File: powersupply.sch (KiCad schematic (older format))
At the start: 18 parts, among them P1 PWR, P2 PWR_SW, U1 LM7805, U2 LM3940

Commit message: Everything associated except joystick
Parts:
- F1: footprint (none) -> SMD_Packages:SMD-1812_l
- P2: footprint (none) -> nu9j-footprints:PWR2-16AWG
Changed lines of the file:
@@
 F 0 "P2" V 3700 2200 40  0000 C CNN
 F 1 "PWR_SW" V 3800 2200 40  0000 C CNN
-F 2 "" H 3750 2200 60  0001 C CNN
+F 2 "nu9j-footprints:PWR2-16AWG" H 3750 2200 60  0001 C CNN
 F 3 "" H 3750 2200 60  0000 C CNN
 	1    3750 2200
@@
 	3300 2550 3650 2550
 $Comp
-L GND #PWR20
+L GND #PWR020
 U 1 1 5470C747
 P 3100 2700
-F 0 "#PWR20" H 3100 2700 30  0001 C CNN
+F 0 "#PWR020" H 3100 2700 30  0001 C CNN
 F 1 "GND" H 3100 2630 30  0001 C CNN
 F 2 "" H 3100 2700 60  0000 C CNN
@@
 $EndComp
 $Comp
-L GND #PWR25
+L GND #PWR021
 U 1 1 5470C830
 P 4450 3000
-F 0 "#PWR25" H 4450 3000 30  0001 C CNN
+F 0 "#PWR021" H 4450 3000 30  0001 C CNN
 F 1 "GND" H 4450 2930 30  0001 C CNN
 F 2 "" H 4450 3000 60  0000 C CNN
@@
 $EndComp
 $Comp
-L GND #PWR26
+L GND #PWR022
 U 1 1 5470C83B
 P 4750 3000
-F 0 "#PWR26" H 4750 3000 30  0001 C CNN
+F 0 "#PWR022" H 4750 3000 30  0001 C CNN
 F 1 "GND" H 4750 2930 30  0001 C CNN
 F 2 "" H 4750 3000 60  0000 C CNN
@@
 	4750 2950 4750 3000
 $Comp
-L +12V #PWR39
+L +12V #PWR023
 U 1 1 5470C933
 P 7600 2500
-F 0 "#PWR39" H 7600 2450 20  0001 C CNN
+F 0 "#PWR023" H 7600 2450 20  0001 C CNN
 F 1 "+12V" H 7600 2600 30  0000 C CNN
 F 2 "" H 7600 2500 60  0000 C CNN
@@
 F 0 "F1" H 7250 2600 40  0000 C CNN
 F 1 "PTS181224V150" H 7050 2500 40  0000 C CNN
-F 2 "" H 7150 2550 60  0001 C CNN
+F 2 "SMD_Packages:SMD-1812_l" H 7150 2550 60  0001 C CNN
 F 3 "" H 7150 2550 60  0000 C CNN
 	1    7150 2550
@@
 	7600 2550 7600 2500
 $Comp
-L GND #PWR22
+L GND #PWR024
 U 1 1 5470CBF4
 P 3900 4250
-F 0 "#PWR22" H 3900 4250 30  0001 C CNN
+F 0 "#PWR024" H 3900 4250 30  0001 C CNN
 F 1 "GND" H 3900 4180 30  0001 C CNN
 F 2 "" H 3900 4250 60  0000 C CNN
@@
 $EndComp
 $Comp
-L GND #PWR31
+L GND #PWR025
 U 1 1 5470CBFF
 P 5750 4250
-F 0 "#PWR31" H 5750 4250 30  0001 C CNN
+F 0 "#PWR025" H 5750 4250 30  0001 C CNN
 F 1 "GND" H 5750 4180 30  0001 C CNN
 F 2 "" H 5750 4250 60  0000 C CNN
@@
 $EndComp
 $Comp
-L +12V #PWR21
+L +12V #PWR026
 U 1 1 5470CC17
 P 3500 3950
-F 0 "#PWR21" H 3500 3900 20  0001 C CNN
+F 0 "#PWR026" H 3500 3900 20  0001 C CNN
 F 1 "+12V" H 3500 4050 30  0000 C CNN
 F 2 "" H 3500 3950 60  0000 C CNN
@@
 $EndComp
 $Comp
-L +5V #PWR23
+L +5V #PWR027
 U 1 1 5470CC25
 P 4300 3950
-F 0 "#PWR23" H 4300 4040 20  0001 C CNN
+F 0 "#PWR027" H 4300 4040 20  0001 C CNN
 F 1 "+5V" H 4300 4040 30  0000 C CNN
 F 2 "" H 4300 3950 60  0000 C CNN
@@
 $EndComp
 $Comp
-L +5V #PWR29
+L +5V #PWR028
 U 1 1 5470CC37
 P 5350 3950
-F 0 "#PWR29" H 5350 4040 20  0001 C CNN
+F 0 "#PWR028" H 5350 4040 20  0001 C CNN
 F 1 "+5V" H 5350 4040 30  0000 C CNN
 F 2 "" H 5350 3950 60  0000 C CNN
@@
 $EndComp
 $Comp
-L +3.3V #PWR34
+L +3.3V #PWR029
 U 1 1 5470CC44
 P 6150 3950
-F 0 "#PWR34" H 6150 3910 30  0001 C CNN
+F 0 "#PWR029" H 6150 3910 30  0001 C CNN
 F 1 "+3.3V" H 6150 4060 30  0000 C CNN
 F 2 "" H 6150 3950 60  0000 C CNN
@@
 $EndComp
 $Comp
-L GND #PWR24
+L GND #PWR030
 U 1 1 5470CCF4
 P 4300 4350
-F 0 "#PWR24" H 4300 4350 30  0001 C CNN
+F 0 "#PWR030" H 4300 4350 30  0001 C CNN
 F 1 "GND" H 4300 4280 30  0001 C CNN
 F 2 "" H 4300 4350 60  0000 C CNN
@@
 $EndComp
 $Comp
-L GND #PWR35
+L GND #PWR031
 U 1 1 5470CCFF
 P 6150 4350
-F 0 "#PWR35" H 6150 4350 30  0001 C CNN
+F 0 "#PWR031" H 6150 4350 30  0001 C CNN
 F 1 "GND" H 6150 4280 30  0001 C CNN
 F 2 "" H 6150 4350 60  0000 C CNN
@@
 $EndComp
 $Comp
-L GND #PWR27
+L GND #PWR032
 U 1 1 54789812
 P 5050 3000
-F 0 "#PWR27" H 5050 3000 30  0001 C CNN
+F 0 "#PWR032" H 5050 3000 30  0001 C CNN
 F 1 "GND" H 5050 2930 30  0001 C CNN
 F 2 "" H 5050 3000 60  0000 C CNN
@@
 $EndComp
 $Comp
-L GND #PWR28
+L GND #PWR033
 U 1 1 5478981D
 P 5350 3000
-F 0 "#PWR28" H 5350 3000 30  0001 C CNN
+F 0 "#PWR033" H 5350 3000 30  0001 C CNN
 F 1 "GND" H 5350 2930 30  0001 C CNN
 F 2 "" H 5350 3000 60  0000 C CNN
@@
 $EndComp
 $Comp
-L GND #PWR30
+L GND #PWR034
 U 1 1 54789828
 P 5650 3000
-F 0 "#PWR30" H 5650 3000 30  0001 C CNN
+F 0 "#PWR034" H 5650 3000 30  0001 C CNN
 F 1 "GND" H 5650 2930 30  0001 C CNN
 F 2 "" H 5650 3000 60  0000 C CNN
@@
 $EndComp
 $Comp
-L GND #PWR32
+L GND #PWR035
 U 1 1 54789833
 P 5900 3000
-F 0 "#PWR32" H 5900 3000 30  0001 C CNN
+F 0 "#PWR035" H 5900 3000 30  0001 C CNN
 F 1 "GND" H 5900 2930 30  0001 C CNN
 F 2 "" H 5900 3000 60  0000 C CNN
@@
 $EndComp
 $Comp
-L GND #PWR33
+L GND #PWR036
 U 1 1 5478983E
 P 6100 3000
-F 0 "#PWR33" H 6100 3000 30  0001 C CNN
+F 0 "#PWR036" H 6100 3000 30  0001 C CNN
 F 1 "GND" H 6100 2930 30  0001 C CNN
 F 2 "" H 6100 3000 60  0000 C CNN
@@
 $EndComp
 $Comp
-L GND #PWR36
+L GND #PWR037
 U 1 1 54789849
 P 6300 3000
-F 0 "#PWR36" H 6300 3000 30  0001 C CNN
+F 0 "#PWR037" H 6300 3000 30  0001 C CNN
 F 1 "GND" H 6300 2930 30  0001 C CNN
 F 2 "" H 6300 3000 60  0000 C CNN
@@
 $EndComp
 $Comp
-L GND #PWR37
+L GND #PWR038
 U 1 1 54789854
 P 6500 3000
-F 0 "#PWR37" H 6500 3000 30  0001 C CNN
+F 0 "#PWR038" H 6500 3000 30  0001 C CNN
 F 1 "GND" H 6500 2930 30  0001 C CNN
 F 2 "" H 6500 3000 60  0000 C CNN
@@
 $EndComp
 $Comp
-L GND #PWR38
+L GND #PWR039
 U 1 1 5478985F
 P 6700 3000
-F 0 "#PWR38" H 6700 3000 30  0001 C CNN
+F 0 "#PWR039" H 6700 3000 30  0001 C CNN
 F 1 "GND" H 6700 2930 30  0001 C CNN
 F 2 "" H 6700 3000 60  0000 C CNN

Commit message: Fixed pin assignment issues in pcb layout
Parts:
- U1: footprint SMD_Packages:DPAK-2 -> nu9j-footprints:DPAK-3_VIVOGND
- U2: footprint SMD_Packages:TO-263 -> nu9j-footprints:TO-263_VIVOGND
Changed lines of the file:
@@
 F 0 "U1" H 4050 3804 60  0000 C CNN
 F 1 "LM7805" H 3900 4200 60  0000 C CNN
-F 2 "SMD_Packages:DPAK-2" H 3900 4000 60  0001 C CNN
+F 2 "nu9j-footprints:DPAK-3_VIVOGND" H 3900 4000 60  0001 C CNN
 F 3 "" H 3900 4000 60  0000 C CNN
 	1    3900 4000
@@
 F 0 "U2" H 5900 3804 60  0000 C CNN
 F 1 "LM3940" H 5750 4200 60  0000 C CNN
-F 2 "SMD_Packages:TO-263" H 5750 4000 60  0001 C CNN
+F 2 "nu9j-footprints:TO-263_VIVOGND" H 5750 4000 60  0001 C CNN
 F 3 "" H 5750 4000 60  0000 C CNN
 	1    5750 4000

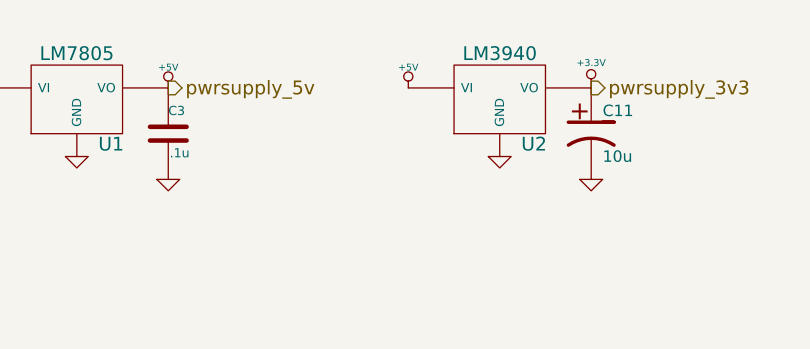
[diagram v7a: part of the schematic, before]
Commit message: Separate analog/digital gnd. Add some filtering caps and reset button.
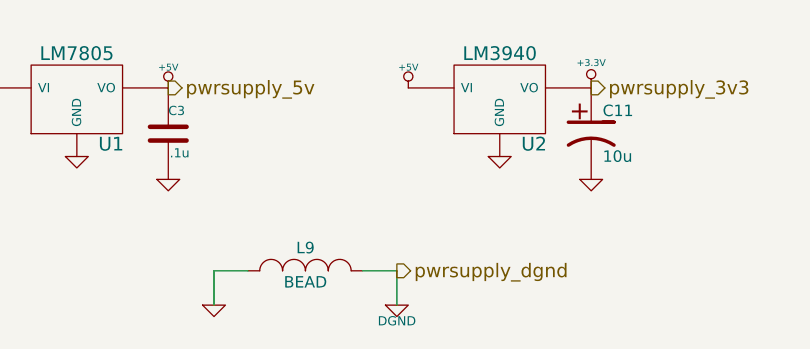
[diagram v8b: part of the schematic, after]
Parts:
- added L9: BEAD, nu9j-footprints:WE-SUCKW, symbol INDUCTOR_SMALL
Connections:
- net GND: now also L9.1
- new net DGND: L9.2
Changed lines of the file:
@@
 	3300 2550 3650 2550
 $Comp
-L GND #PWR020
+L GND #PWR021
 U 1 1 5470C747
 P 3100 2700
-F 0 "#PWR020" H 3100 2700 30  0001 C CNN
+F 0 "#PWR021" H 3100 2700 30  0001 C CNN
 F 1 "GND" H 3100 2630 30  0001 C CNN
 F 2 "" H 3100 2700 60  0000 C CNN
@@
 $EndComp
 $Comp
-L GND #PWR021
+L GND #PWR022
 U 1 1 5470C830
 P 4450 3000
-F 0 "#PWR021" H 4450 3000 30  0001 C CNN
+F 0 "#PWR022" H 4450 3000 30  0001 C CNN
 F 1 "GND" H 4450 2930 30  0001 C CNN
 F 2 "" H 4450 3000 60  0000 C CNN
@@
 $EndComp
 $Comp
-L GND #PWR022
+L GND #PWR023
 U 1 1 5470C83B
 P 4750 3000
-F 0 "#PWR022" H 4750 3000 30  0001 C CNN
+F 0 "#PWR023" H 4750 3000 30  0001 C CNN
 F 1 "GND" H 4750 2930 30  0001 C CNN
 F 2 "" H 4750 3000 60  0000 C CNN
@@
 	4750 2950 4750 3000
 $Comp
-L +12V #PWR023
+L +12V #PWR024
 U 1 1 5470C933
 P 7600 2500
-F 0 "#PWR023" H 7600 2450 20  0001 C CNN
+F 0 "#PWR024" H 7600 2450 20  0001 C CNN
 F 1 "+12V" H 7600 2600 30  0000 C CNN
 F 2 "" H 7600 2500 60  0000 C CNN
@@
 	7600 2550 7600 2500
 $Comp
-L GND #PWR024
+L GND #PWR025
 U 1 1 5470CBF4
 P 3900 4250
-F 0 "#PWR024" H 3900 4250 30  0001 C CNN
+F 0 "#PWR025" H 3900 4250 30  0001 C CNN
 F 1 "GND" H 3900 4180 30  0001 C CNN
 F 2 "" H 3900 4250 60  0000 C CNN
@@
 $EndComp
 $Comp
-L GND #PWR025
+L GND #PWR026
 U 1 1 5470CBFF
 P 5750 4250
-F 0 "#PWR025" H 5750 4250 30  0001 C CNN
+F 0 "#PWR026" H 5750 4250 30  0001 C CNN
 F 1 "GND" H 5750 4180 30  0001 C CNN
 F 2 "" H 5750 4250 60  0000 C CNN
@@
 $EndComp
 $Comp
-L +12V #PWR026
+L +12V #PWR027
 U 1 1 5470CC17
 P 3500 3950
-F 0 "#PWR026" H 3500 3900 20  0001 C CNN
+F 0 "#PWR027" H 3500 3900 20  0001 C CNN
 F 1 "+12V" H 3500 4050 30  0000 C CNN
 F 2 "" H 3500 3950 60  0000 C CNN
@@
 $EndComp
 $Comp
-L +5V #PWR027
+L +5V #PWR028
 U 1 1 5470CC25
 P 4300 3950
-F 0 "#PWR027" H 4300 4040 20  0001 C CNN
+F 0 "#PWR028" H 4300 4040 20  0001 C CNN
 F 1 "+5V" H 4300 4040 30  0000 C CNN
 F 2 "" H 4300 3950 60  0000 C CNN
@@
 $EndComp
 $Comp
-L +5V #PWR028
+L +5V #PWR029
 U 1 1 5470CC37
 P 5350 3950
-F 0 "#PWR028" H 5350 4040 20  0001 C CNN
+F 0 "#PWR029" H 5350 4040 20  0001 C CNN
 F 1 "+5V" H 5350 4040 30  0000 C CNN
 F 2 "" H 5350 3950 60  0000 C CNN
@@
 $EndComp
 $Comp
-L +3.3V #PWR029
+L +3.3V #PWR030
 U 1 1 5470CC44
 P 6150 3950
-F 0 "#PWR029" H 6150 3910 30  0001 C CNN
+F 0 "#PWR030" H 6150 3910 30  0001 C CNN
 F 1 "+3.3V" H 6150 4060 30  0000 C CNN
 F 2 "" H 6150 3950 60  0000 C CNN
@@
 $EndComp
 $Comp
-L GND #PWR030
+L GND #PWR031
 U 1 1 5470CCF4
 P 4300 4350
-F 0 "#PWR030" H 4300 4350 30  0001 C CNN
+F 0 "#PWR031" H 4300 4350 30  0001 C CNN
 F 1 "GND" H 4300 4280 30  0001 C CNN
 F 2 "" H 4300 4350 60  0000 C CNN
@@
 $EndComp
 $Comp
-L GND #PWR031
+L GND #PWR032
 U 1 1 5470CCFF
 P 6150 4350
-F 0 "#PWR031" H 6150 4350 30  0001 C CNN
+F 0 "#PWR032" H 6150 4350 30  0001 C CNN
 F 1 "GND" H 6150 4280 30  0001 C CNN
 F 2 "" H 6150 4350 60  0000 C CNN
@@
 $EndComp
 $Comp
-L GND #PWR032
+L GND #PWR033
 U 1 1 54789812
 P 5050 3000
-F 0 "#PWR032" H 5050 3000 30  0001 C CNN
+F 0 "#PWR033" H 5050 3000 30  0001 C CNN
 F 1 "GND" H 5050 2930 30  0001 C CNN
 F 2 "" H 5050 3000 60  0000 C CNN
@@
 $EndComp
 $Comp
-L GND #PWR033
+L GND #PWR034
 U 1 1 5478981D
 P 5350 3000
-F 0 "#PWR033" H 5350 3000 30  0001 C CNN
+F 0 "#PWR034" H 5350 3000 30  0001 C CNN
 F 1 "GND" H 5350 2930 30  0001 C CNN
 F 2 "" H 5350 3000 60  0000 C CNN
@@
 $EndComp
 $Comp
-L GND #PWR034
+L GND #PWR035
 U 1 1 54789828
 P 5650 3000
-F 0 "#PWR034" H 5650 3000 30  0001 C CNN
+F 0 "#PWR035" H 5650 3000 30  0001 C CNN
 F 1 "GND" H 5650 2930 30  0001 C CNN
 F 2 "" H 5650 3000 60  0000 C CNN
@@
 $EndComp
 $Comp
-L GND #PWR035
+L GND #PWR036
 U 1 1 54789833
 P 5900 3000
-F 0 "#PWR035" H 5900 3000 30  0001 C CNN
+F 0 "#PWR036" H 5900 3000 30  0001 C CNN
 F 1 "GND" H 5900 2930 30  0001 C CNN
 F 2 "" H 5900 3000 60  0000 C CNN
@@
 $EndComp
 $Comp
-L GND #PWR036
+L GND #PWR037
 U 1 1 5478983E
 P 6100 3000
-F 0 "#PWR036" H 6100 3000 30  0001 C CNN
+F 0 "#PWR037" H 6100 3000 30  0001 C CNN
 F 1 "GND" H 6100 2930 30  0001 C CNN
 F 2 "" H 6100 3000 60  0000 C CNN
@@
 $EndComp
 $Comp
-L GND #PWR037
+L GND #PWR038
 U 1 1 54789849
 P 6300 3000
-F 0 "#PWR037" H 6300 3000 30  0001 C CNN
+F 0 "#PWR038" H 6300 3000 30  0001 C CNN
 F 1 "GND" H 6300 2930 30  0001 C CNN
 F 2 "" H 6300 3000 60  0000 C CNN
@@
 $EndComp
 $Comp
-L GND #PWR038
+L GND #PWR039
 U 1 1 54789854
 P 6500 3000
-F 0 "#PWR038" H 6500 3000 30  0001 C CNN
+F 0 "#PWR039" H 6500 3000 30  0001 C CNN
 F 1 "GND" H 6500 2930 30  0001 C CNN
 F 2 "" H 6500 3000 60  0000 C CNN
@@
 $EndComp
 $Comp
-L GND #PWR039
+L GND #PWR040
 U 1 1 5478985F
 P 6700 3000
-F 0 "#PWR039" H 6700 3000 30  0001 C CNN
+F 0 "#PWR040" H 6700 3000 30  0001 C CNN
 F 1 "GND" H 6700 2930 30  0001 C CNN
 F 2 "" H 6700 3000 60  0000 C CNN
@@
 Wire Wire Line
 	6700 2950 6700 3000
+$Comp
+L INDUCTOR_SMALL L9
+U 1 1 548467CE
+P 4900 4750
+F 0 "L9" H 4900 4850 50  0000 C CNN
+F 1 "BEAD" H 4900 4700 50  0000 C CNN
+F 2 "nu9j-footprints:WE-SUCKW" H 4900 4750 60  0001 C CNN
+F 3 "" H 4900 4750 60  0000 C CNN
+	1    4900 4750
+	1    0    0    -1
+$EndComp
+$Comp
+L GND #PWR041
+U 1 1 54846846
+P 4500 4900
+F 0 "#PWR041" H 4500 4900 30  0001 C CNN
+F 1 "GND" H 4500 4830 30  0001 C CNN
+F 2 "" H 4500 4900 60  0000 C CNN
+F 3 "" H 4500 4900 60  0000 C CNN
+	1    4500 4900
+	1    0    0    -1
+$EndComp
+$Comp
+L DGND #PWR042
+U 1 1 54846853
+P 5300 4900
+F 0 "#PWR042" H 5300 4900 40  0001 C CNN
+F 1 "DGND" H 5300 4830 40  0000 C CNN
+F 2 "" H 5300 4900 60  0000 C CNN
+F 3 "" H 5300 4900 60  0000 C CNN
+	1    5300 4900
+	1    0    0    -1
+$EndComp
+Wire Wire Line
+	5150 4750 5300 4750
+Wire Wire Line
+	5300 4750 5300 4900
+Wire Wire Line
+	4650 4750 4500 4750
+Wire Wire Line
+	4500 4750 4500 4900
+Text HLabel 5300 4750 2    60   Output ~ 0
+pwrsupply_dgnd
 $EndSCHEMATC
